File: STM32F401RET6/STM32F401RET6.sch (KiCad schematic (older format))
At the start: 12 parts

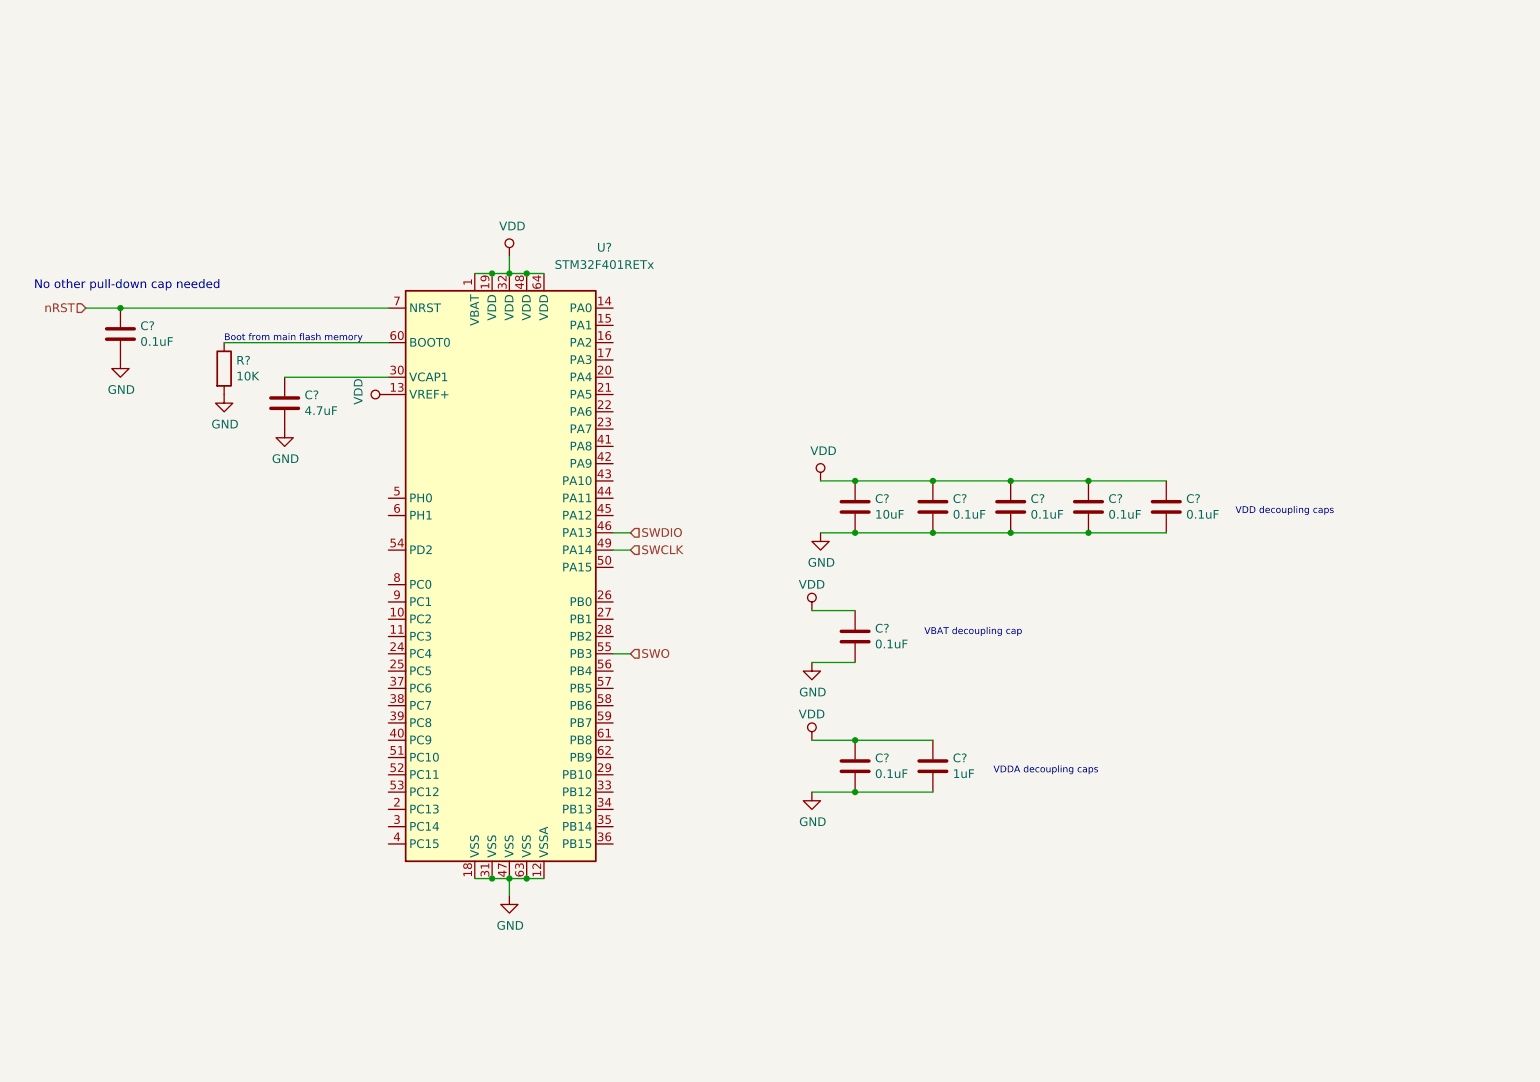
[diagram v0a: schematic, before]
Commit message: added hierarchical pins and descriptions
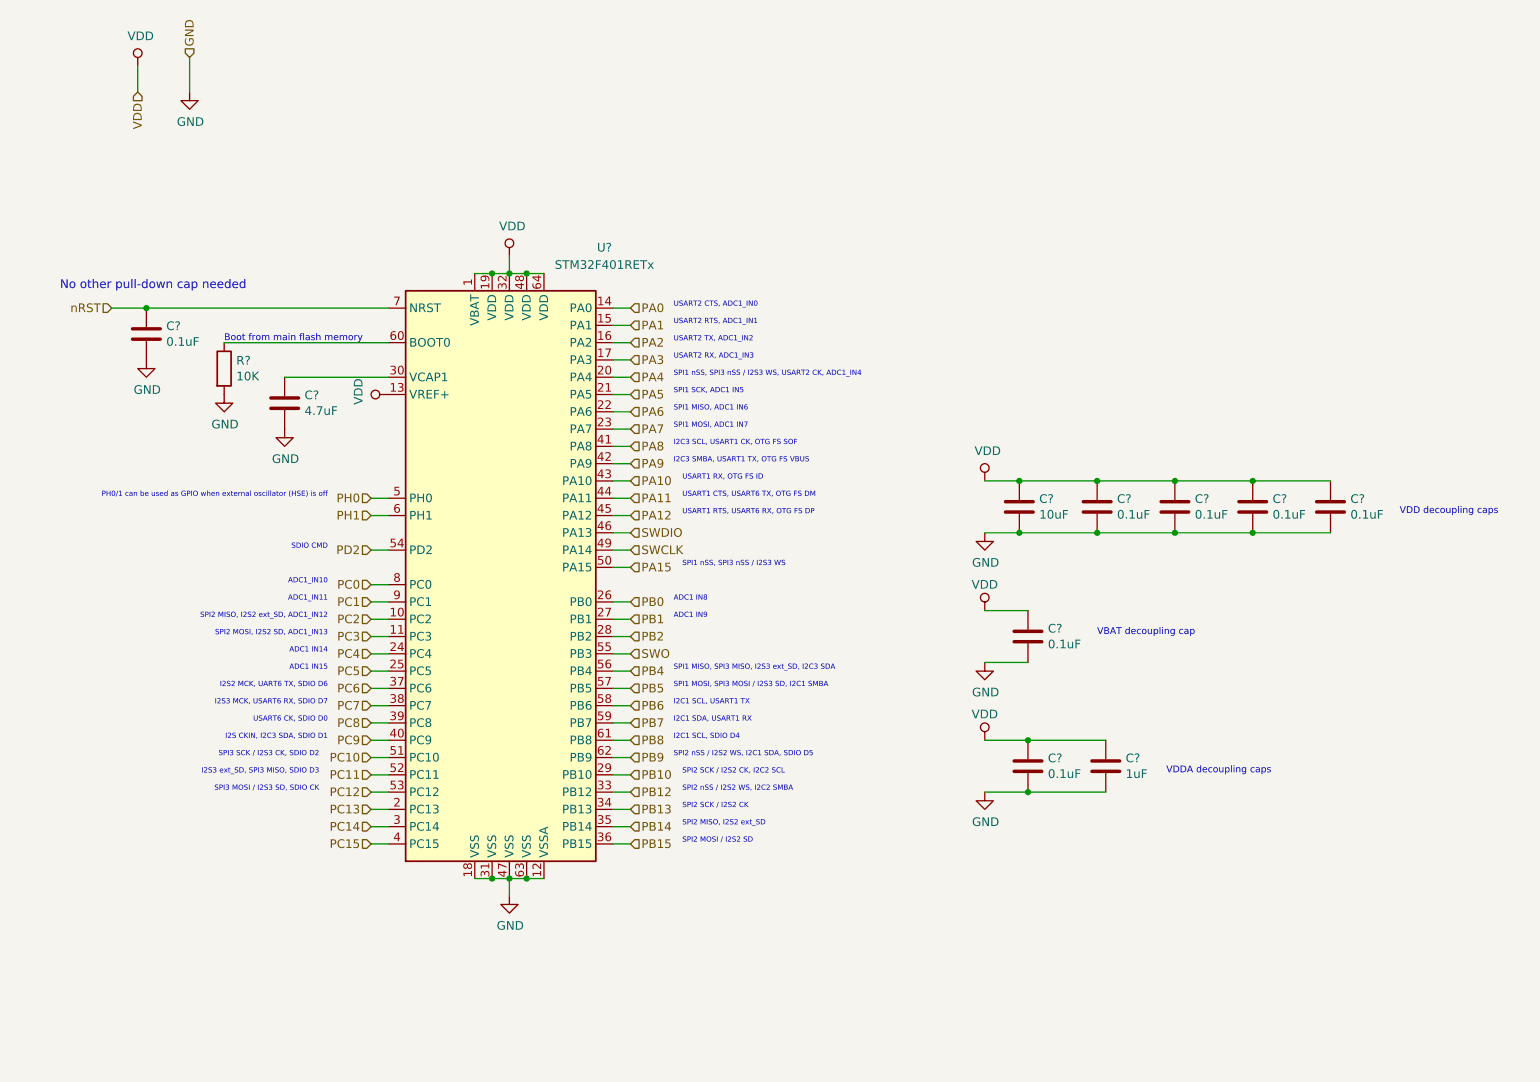
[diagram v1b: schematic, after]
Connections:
- net PC2: now reaches U?.10 (PC2)
- net PC3: now reaches U?.11 (PC3)
- net PA0: now reaches U?.14 (PA0)
- net PA1: now reaches U?.15 (PA1)
- net PA2: now reaches U?.16 (PA2)
- net PA3: now reaches U?.17 (PA3)
- net PC13: now reaches U?.2 (PC13)
- net PA4: now reaches U?.20 (PA4)
- net PA5: now reaches U?.21 (PA5)
- net PA6: now reaches U?.22 (PA6)
- net PA7: now reaches U?.23 (PA7)
- net PC4: now reaches U?.24 (PC4)
- net PC5: now reaches U?.25 (PC5)
- net PB0: now reaches U?.26 (PB0)
- net PB1: now reaches U?.27 (PB1)
- net PB2: now reaches U?.28 (PB2)
- net PB10: now reaches U?.29 (PB10)
- net PC14: now reaches U?.3 (PC14)
- net PB12: now reaches U?.33 (PB12)
- net PB13: now reaches U?.34 (PB13)
- net PB14: now reaches U?.35 (PB14)
- net PB15: now reaches U?.36 (PB15)
- net PC6: now reaches U?.37 (PC6)
- net PC7: now reaches U?.38 (PC7)
- net PC8: now reaches U?.39 (PC8)
- net PC15: now reaches U?.4 (PC15)
- net PC9: now reaches U?.40 (PC9)
- net PA8: now reaches U?.41 (PA8)
- net PA9: now reaches U?.42 (PA9)
- net PA10: now reaches U?.43 (PA10)
- net PA11: now reaches U?.44 (PA11)
- net PA12: now reaches U?.45 (PA12)
- net PH0: now reaches U?.5 (PH0)
- net PA15: now reaches U?.50 (PA15)
- net PC10: now reaches U?.51 (PC10)
- net PC11: now reaches U?.52 (PC11)
- net PC12: now reaches U?.53 (PC12)
- net PD2: now reaches U?.54 (PD2)
- net PB4: now reaches U?.56 (PB4)
- net PB5: now reaches U?.57 (PB5)
- net PB6: now reaches U?.58 (PB6)
- net PB7: now reaches U?.59 (PB7)
- net PH1: now reaches U?.6 (PH1)
- net PB8: now reaches U?.61 (PB8)
- net PB9: now reaches U?.62 (PB9)
- net PC0: now reaches U?.8 (PC0)
- net PC1: now reaches U?.9 (PC1)
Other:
- note added: "ADC1 IN14"
- note added: "ADC1 IN15"
- note added: "ADC1 IN8"
- note added: "ADC1 IN9"
- note added: "ADC1_IN10"
- note added: "ADC1_IN11"
- note added: "I2C1 SCL, SDIO D4"
- note added: "I2C1 SCL, USART1 TX"
- note added: "I2C1 SDA, USART1 RX"
- note added: "I2C3 SCL, USART1 CK, OTG FS SOF"
- note added: "I2C3 SMBA, USART1 TX, OTG FS VBUS"
- note added: "I2S CKIN, I2C3 SDA, SDIO D1"
- note added: "I2S2 MCK, UART6 TX, SDIO D6"
- note added: "I2S3 MCK, USART6 RX, SDIO D7"
- note added: "I2S3 ext_SD, SPI3 MISO, SDIO D3"
- note added: "PH0/1 can be used as GPIO when external oscillator (HSE) is off"
- note added: "SDIO CMD"
- note added: "SPI1 MISO, ADC1 IN6"
- note added: "SPI1 MISO, SPI3 MISO, I2S3 ext_SD, I2C3 SDA"
- note added: "SPI1 MOSI, ADC1 IN7"
- note added: "SPI1 MOSI, SPI3 MOSI / I2S3 SD, I2C1 SMBA"
- note added: "SPI1 SCK, ADC1 IN5"
- note added: "SPI1 nSS, SPI3 nSS / I2S3 WS"
- note added: "SPI1 nSS, SPI3 nSS / I2S3 WS, USART2 CK, ADC1_IN4"
- note added: "SPI2 MISO, I2S2 ext_SD"
- note added: "SPI2 MISO, I2S2 ext_SD, ADC1_IN12"
- note added: "SPI2 MOSI / I2S2 SD"
- note added: "SPI2 MOSI, I2S2 SD, ADC1_IN13"
- note added: "SPI2 SCK / I2S2 CK"
- note added: "SPI2 SCK / I2S2 CK, I2C2 SCL"
- note added: "SPI2 nSS / I2S2 WS, I2C1 SDA, SDIO D5"
- note added: "SPI2 nSS / I2S2 WS, I2C2 SMBA"
- note added: "SPI3 MOSI / I2S3 SD, SDIO CK"
- note added: "SPI3 SCK / I2S3 CK, SDIO D2"
- note added: "USART1 CTS, USART6 TX, OTG FS DM"
- note added: "USART1 RTS, USART6 RX, OTG FS DP"
- note added: "USART1 RX, OTG FS ID"
- note added: "USART2 CTS, ADC1_IN0"
- note added: "USART2 RTS, ADC1_IN1"
- note added: "USART2 RX, ADC1_IN3"
- note added: "USART2 TX, ADC1_IN2"
- note added: "USART6 CK, SDIO D0"
- moved on the sheet: C?

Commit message: now ?
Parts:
- removed C?: 1uF, symbol Device:C
- removed C?: 10uF, symbol Device:C
- removed C? (x7): 0.1uF, symbol Device:C
- removed C?: 4.7uF, symbol Device:C
- removed R?: 10K, symbol Device:R
- removed U?: STM32F401RETx, Package_QFP:LQFP-64_10x10mm_P0.5mm, symbol MCU_ST_STM32F4:STM32F401RETx
- added U?: STM32F401RETx, Package_QFP:LQFP-64_10x10mm_P0.5mm, symbol MCU_ST_STM32F4:STM32F401RETx
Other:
- note removed: "ADC1 IN14"
- note removed: "ADC1 IN15"
- note removed: "ADC1 IN8"
- note removed: "ADC1 IN9"
- note removed: "ADC1_IN10"
- note removed: "ADC1_IN11"
- note removed: "Boot from main flash memory"
- note removed: "I2C1 SCL, SDIO D4"
- note removed: "I2C1 SCL, USART1 TX"
- note removed: "I2C1 SDA, USART1 RX"
- note removed: "I2C3 SCL, USART1 CK, OTG FS SOF"
- note removed: "I2C3 SMBA, USART1 TX, OTG FS VBUS"
- note removed: "I2S CKIN, I2C3 SDA, SDIO D1"
- note removed: "I2S2 MCK, UART6 TX, SDIO D6"
- note removed: "I2S3 MCK, USART6 RX, SDIO D7"
- note removed: "I2S3 ext_SD, SPI3 MISO, SDIO D3"
- note removed: "No other pull-down cap needed"
- note removed: "PH0/1 can be used as GPIO when external oscillator (HSE) is off"
- note removed: "SDIO CMD"
- note removed: "SPI1 MISO, ADC1 IN6"
- note removed: "SPI1 MISO, SPI3 MISO, I2S3 ext_SD, I2C3 SDA"
- note removed: "SPI1 MOSI, ADC1 IN7"
- note removed: "SPI1 MOSI, SPI3 MOSI / I2S3 SD, I2C1 SMBA"
- note removed: "SPI1 SCK, ADC1 IN5"
- note removed: "SPI1 nSS, SPI3 nSS / I2S3 WS"
- note removed: "SPI1 nSS, SPI3 nSS / I2S3 WS, USART2 CK, ADC1_IN4"
- note removed: "SPI2 MISO, I2S2 ext_SD"
- note removed: "SPI2 MISO, I2S2 ext_SD, ADC1_IN12"
- note removed: "SPI2 MOSI / I2S2 SD"
- note removed: "SPI2 MOSI, I2S2 SD, ADC1_IN13"
- note removed: "SPI2 SCK / I2S2 CK"
- note removed: "SPI2 SCK / I2S2 CK, I2C2 SCL"
- note removed: "SPI2 nSS / I2S2 WS, I2C1 SDA, SDIO D5"
- note removed: "SPI2 nSS / I2S2 WS, I2C2 SMBA"
- note removed: "SPI3 MOSI / I2S3 SD, SDIO CK"
- note removed: "SPI3 SCK / I2S3 CK, SDIO D2"
- note removed: "USART1 CTS, USART6 TX, OTG FS DM"
- note removed: "USART1 RTS, USART6 RX, OTG FS DP"
- note removed: "USART1 RX, OTG FS ID"
- note removed: "USART2 CTS, ADC1_IN0"
- note removed: "USART2 RTS, ADC1_IN1"
- note removed: "USART2 RX, ADC1_IN3"
- note removed: "USART2 TX, ADC1_IN2"
- note removed: "USART6 CK, SDIO D0"
- note removed: "VBAT decoupling cap"
- note removed: "VDD decoupling caps"
- note removed: "VDDA decoupling caps\n"

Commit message: test with generated .lib
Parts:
- removed U?: STM32F401RETx, Package_QFP:LQFP-64_10x10mm_P0.5mm, symbol MCU_ST_STM32F4:STM32F401RETx
- added C?: 1uF, symbol Device:C
- added C?: 10uF, symbol Device:C
- added C? (x7): 0.1uF, symbol Device:C
- added C?: 4.7uF, symbol Device:C
- added R?: 10K, symbol Device:R
- added U?: STM32F401RETx, Package_QFP:LQFP-64_10x10mm_P0.5mm, symbol MCU_ST_STM32F4:STM32F401RETx
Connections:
- new net: C?.1, U?.30 (VCAP1)
- new net: R?.1, U?.60 (BOOT0)
- new net GND: C?.2, C?.2, C?.2, C?.2, C?.2, C?.2, C?.2, C?.2, C?.2, C?.2, R?.2, U?.12 (VSSA), U?.18 (VSS), U?.31 (VSS), U?.47 (VSS), U?.63 (VSS)
- new net PA0: U?.14 (PA0)
- new net PA1: U?.15 (PA1)
- new net PA10: U?.43 (PA10)
- new net PA11: U?.44 (PA11)
- new net PA12: U?.45 (PA12)
- new net PA15: U?.50 (PA15)
- new net PA2: U?.16 (PA2)
- new net PA3: U?.17 (PA3)
- new net PA4: U?.20 (PA4)
- new net PA5: U?.21 (PA5)
- new net PA6: U?.22 (PA6)
- new net PA7: U?.23 (PA7)
- new net PA8: U?.41 (PA8)
- new net PA9: U?.42 (PA9)
- new net PB0: U?.26 (PB0)
- new net PB1: U?.27 (PB1)
- new net PB10: U?.29 (PB10)
- new net PB12: U?.33 (PB12)
- new net PB13: U?.34 (PB13)
- new net PB14: U?.35 (PB14)
- new net PB15: U?.36 (PB15)
- new net PB2: U?.28 (PB2)
- new net PB4: U?.56 (PB4)
- new net PB5: U?.57 (PB5)
- new net PB6: U?.58 (PB6)
- new net PB7: U?.59 (PB7)
- new net PB8: U?.61 (PB8)
- new net PB9: U?.62 (PB9)
- new net PC0: U?.8 (PC0)
- new net PC1: U?.9 (PC1)
- new net PC10: U?.51 (PC10)
- new net PC11: U?.52 (PC11)
- new net PC12: U?.53 (PC12)
- new net PC13: U?.2 (PC13)
- new net PC14: U?.3 (PC14)
- new net PC15: U?.4 (PC15)
- new net PC2: U?.10 (PC2)
- new net PC3: U?.11 (PC3)
- new net PC4: U?.24 (PC4)
- new net PC5: U?.25 (PC5)
- new net PC6: U?.37 (PC6)
- new net PC7: U?.38 (PC7)
- new net PC8: U?.39 (PC8)
- new net PC9: U?.40 (PC9)
- new net PD2: U?.54 (PD2)
- new net PH0: U?.5 (PH0)
- new net PH1: U?.6 (PH1)
- new net SWCLK: U?.49 (PA14)
- new net SWDIO: U?.46 (PA13)
- new net SWO: U?.55 (PB3)
- new net VDD: C?.1, C?.1, C?.1, C?.1, C?.1, C?.1, C?.1, C?.1, U?.1 (VBAT), U?.13 (VREF+), U?.19 (VDD), U?.32 (VDD), U?.48 (VDD), U?.64 (VDD)
- new net nRST: C?.1, U?.7 (NRST)
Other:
- note added: "ADC1 IN14"
- note added: "ADC1 IN15"
- note added: "ADC1 IN8"
- note added: "ADC1 IN9"
- note added: "ADC1_IN10"
- note added: "ADC1_IN11"
- note added: "Boot from main flash memory"
- note added: "I2C1 SCL, SDIO D4"
- note added: "I2C1 SCL, USART1 TX"
- note added: "I2C1 SDA, USART1 RX"
- note added: "I2C3 SCL, USART1 CK, OTG FS SOF"
- note added: "I2C3 SMBA, USART1 TX, OTG FS VBUS"
- note added: "I2S CKIN, I2C3 SDA, SDIO D1"
- note added: "I2S2 MCK, UART6 TX, SDIO D6"
- note added: "I2S3 MCK, USART6 RX, SDIO D7"
- note added: "I2S3 ext_SD, SPI3 MISO, SDIO D3"
- note added: "No other pull-down cap needed"
- note added: "PH0/1 can be used as GPIO when external oscillator (HSE) is off"
- note added: "SDIO CMD"
- note added: "SPI1 MISO, ADC1 IN6"
- note added: "SPI1 MISO, SPI3 MISO, I2S3 ext_SD, I2C3 SDA"
- note added: "SPI1 MOSI, ADC1 IN7"
- note added: "SPI1 MOSI, SPI3 MOSI / I2S3 SD, I2C1 SMBA"
- note added: "SPI1 SCK, ADC1 IN5"
- note added: "SPI1 nSS, SPI3 nSS / I2S3 WS"
- note added: "SPI1 nSS, SPI3 nSS / I2S3 WS, USART2 CK, ADC1_IN4"
- note added: "SPI2 MISO, I2S2 ext_SD"
- note added: "SPI2 MISO, I2S2 ext_SD, ADC1_IN12"
- note added: "SPI2 MOSI / I2S2 SD"
- note added: "SPI2 MOSI, I2S2 SD, ADC1_IN13"
- note added: "SPI2 SCK / I2S2 CK"
- note added: "SPI2 SCK / I2S2 CK, I2C2 SCL"
- note added: "SPI2 nSS / I2S2 WS, I2C1 SDA, SDIO D5"
- note added: "SPI2 nSS / I2S2 WS, I2C2 SMBA"
- note added: "SPI3 MOSI / I2S3 SD, SDIO CK"
- note added: "SPI3 SCK / I2S3 CK, SDIO D2"
- note added: "USART1 CTS, USART6 TX, OTG FS DM"
- note added: "USART1 RTS, USART6 RX, OTG FS DP"
- note added: "USART1 RX, OTG FS ID"
- note added: "USART2 CTS, ADC1_IN0"
- note added: "USART2 RTS, ADC1_IN1"
- note added: "USART2 RX, ADC1_IN3"
- note added: "USART2 TX, ADC1_IN2"
- note added: "USART6 CK, SDIO D0"
- note added: "VBAT decoupling cap"
- note added: "VDD decoupling caps"
- note added: "VDDA decoupling caps\n"

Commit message: created from proj
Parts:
- removed C?: 1uF, symbol Device:C
- removed C?: 10uF, symbol Device:C
- removed C? (x7): 0.1uF, symbol Device:C
- removed C?: 4.7uF, symbol Device:C
- removed R?: 10K, symbol Device:R
- removed U?: STM32F401RETx, Package_QFP:LQFP-64_10x10mm_P0.5mm, symbol MCU_ST_STM32F4:STM32F401RETx
- added U?: STM32F401RETx, Package_QFP:LQFP-64_10x10mm_P0.5mm, symbol MCU_ST_STM32F4:STM32F401RETx
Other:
- note removed: "ADC1 IN14"
- note removed: "ADC1 IN15"
- note removed: "ADC1 IN8"
- note removed: "ADC1 IN9"
- note removed: "ADC1_IN10"
- note removed: "ADC1_IN11"
- note removed: "Boot from main flash memory"
- note removed: "I2C1 SCL, SDIO D4"
- note removed: "I2C1 SCL, USART1 TX"
- note removed: "I2C1 SDA, USART1 RX"
- note removed: "I2C3 SCL, USART1 CK, OTG FS SOF"
- note removed: "I2C3 SMBA, USART1 TX, OTG FS VBUS"
- note removed: "I2S CKIN, I2C3 SDA, SDIO D1"
- note removed: "I2S2 MCK, UART6 TX, SDIO D6"
- note removed: "I2S3 MCK, USART6 RX, SDIO D7"
- note removed: "I2S3 ext_SD, SPI3 MISO, SDIO D3"
- note removed: "No other pull-down cap needed"
- note removed: "PH0/1 can be used as GPIO when external oscillator (HSE) is off"
- note removed: "SDIO CMD"
- note removed: "SPI1 MISO, ADC1 IN6"
- note removed: "SPI1 MISO, SPI3 MISO, I2S3 ext_SD, I2C3 SDA"
- note removed: "SPI1 MOSI, ADC1 IN7"
- note removed: "SPI1 MOSI, SPI3 MOSI / I2S3 SD, I2C1 SMBA"
- note removed: "SPI1 SCK, ADC1 IN5"
- note removed: "SPI1 nSS, SPI3 nSS / I2S3 WS"
- note removed: "SPI1 nSS, SPI3 nSS / I2S3 WS, USART2 CK, ADC1_IN4"
- note removed: "SPI2 MISO, I2S2 ext_SD"
- note removed: "SPI2 MISO, I2S2 ext_SD, ADC1_IN12"
- note removed: "SPI2 MOSI / I2S2 SD"
- note removed: "SPI2 MOSI, I2S2 SD, ADC1_IN13"
- note removed: "SPI2 SCK / I2S2 CK"
- note removed: "SPI2 SCK / I2S2 CK, I2C2 SCL"
- note removed: "SPI2 nSS / I2S2 WS, I2C1 SDA, SDIO D5"
- note removed: "SPI2 nSS / I2S2 WS, I2C2 SMBA"
- note removed: "SPI3 MOSI / I2S3 SD, SDIO CK"
- note removed: "SPI3 SCK / I2S3 CK, SDIO D2"
- note removed: "USART1 CTS, USART6 TX, OTG FS DM"
- note removed: "USART1 RTS, USART6 RX, OTG FS DP"
- note removed: "USART1 RX, OTG FS ID"
- note removed: "USART2 CTS, ADC1_IN0"
- note removed: "USART2 RTS, ADC1_IN1"
- note removed: "USART2 RX, ADC1_IN3"
- note removed: "USART2 TX, ADC1_IN2"
- note removed: "USART6 CK, SDIO D0"
- note removed: "VBAT decoupling cap"
- note removed: "VDD decoupling caps"
- note removed: "VDDA decoupling caps\n"
